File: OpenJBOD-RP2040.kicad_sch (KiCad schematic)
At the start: 55 parts, among them J1 ATX-24, J2 Bus_PCI_Express_x1, J3 Conn_02x02_Counter_Clockwise, J8 USB_B_Micro, J9 TEMP1, Q1 MMBT3904, Q2 MMBT3904, SW1 SW_Push, SW2 SW_Push, U1 RP2040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

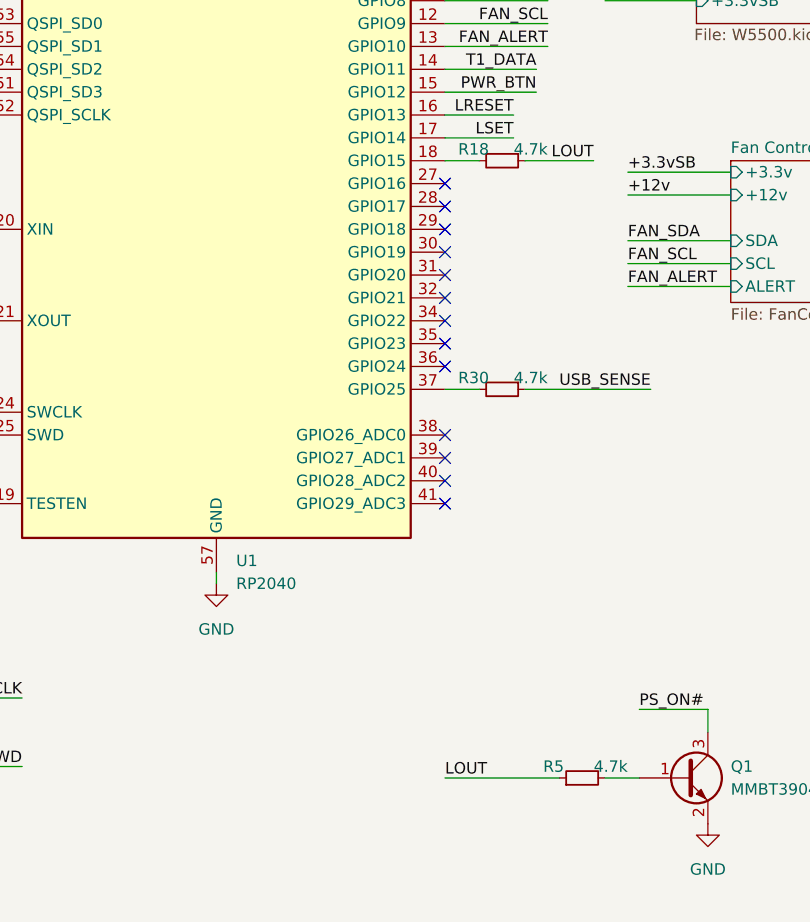
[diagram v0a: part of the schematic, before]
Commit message: added uart header
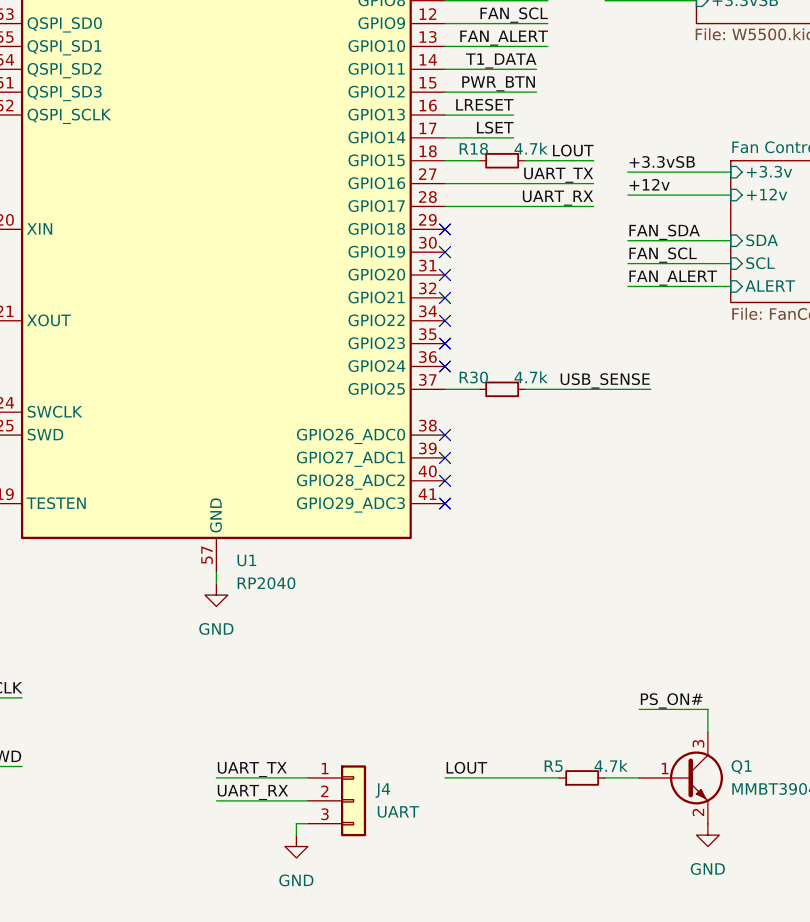
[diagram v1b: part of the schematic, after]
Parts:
- added J4: UART, Connector_PinHeader_2.54mm:PinHeader_1x03_P2.54mm_Vertical, symbol Connector_Generic:Conn_01x03
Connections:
- net GND: now also J4.3 (Pin_3)
- net UART_TX: now reaches U1.27 (GPIO16)
- net UART_TX: now also J4.1 (Pin_1)
- net UART_RX: now reaches U1.28 (GPIO17)
- net UART_RX: now also J4.2 (Pin_2)
- no-connect marks 34 -> 32
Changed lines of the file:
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@@
 	)
 	(no_connect
-		(at 96.52 116.84)
-	)
-	(no_connect
 		(at 247.65 35.56)
 	)
@@
 	)
 	(no_connect
-		(at 96.52 119.38)
-	)
-	(no_connect
 		(at 96.52 124.46)
 	)
@@
 	(wire
 		(pts
+			(xy 96.52 119.38) (xy 113.03 119.38)
+		)
+		(stroke
+			(width 0)
+			(type default)
+		)
+	)
+	(wire
+		(pts
 			(xy 242.57 17.78) (xy 260.35 17.78)
 		)
@@
 	(wire
 		(pts
+			(xy 96.52 116.84) (xy 113.03 116.84)
+		)
+		(stroke
+			(width 0)
+			(type default)
+		)
+	)
+	(wire
+		(pts
+			(xy 71.12 182.88) (xy 81.28 182.88)
+		)
+		(stroke
+			(width 0)
+			(type default)
+		)
+	)
+	(wire
+		(pts
 			(xy 105.41 114.3) (xy 113.03 114.3)
 		)
@@
 	(wire
 		(pts
+			(xy 80.01 189.23) (xy 80.01 187.96)
+		)
+		(stroke
+			(width 0)
+			(type default)
+		)
+	)
+	(wire
+		(pts
 			(xy 231.14 135.89) (xy 243.84 135.89)
 		)
@@
 	(wire
 		(pts
+			(xy 71.12 185.42) (xy 81.28 185.42)
+		)
+		(stroke
+			(width 0)
+			(type default)
+		)
+	)
+	(wire
+		(pts
 			(xy 96.52 81.28) (xy 124.46 81.28)
 		)
@@
 	(wire
 		(pts
+			(xy 80.01 187.96) (xy 81.28 187.96)
+		)
+		(stroke
+			(width 0)
+			(type default)
+		)
+	)
+	(wire
+		(pts
 			(xy 245.11 40.64) (xy 245.11 41.91)
 		)
@@
 		)
 	)
+	(label "UART_RX"
+		(at 113.03 119.38 180)
+		(fields_autoplaced yes)
+		(effects
+			(font
+				(size 1.27 1.27)
+			)
+			(justify right bottom)
+		)
+	)
 	(label "QSPI_SD2"
 		(at 210.82 82.55 0)
@@
 		)
 	)
+	(label "UART_TX"
+		(at 113.03 116.84 180)
+		(fields_autoplaced yes)
+		(effects
+			(font
+				(size 1.27 1.27)
+			)
+			(justify right bottom)
+		)
+	)
 	(label "PS_ON#"
 		(at 185.42 25.4 0)
@@
 		)
 	)
+	(label "UART_TX"
+		(at 71.12 182.88 0)
+		(fields_autoplaced yes)
+		(effects
+			(font
+				(size 1.27 1.27)
+			)
+			(justify left bottom)
+		)
+	)
 	(label "PWR_BTN"
 		(at 146.05 185.42 0)
@@
 		)
 	)
+	(label "UART_RX"
+		(at 71.12 185.42 0)
+		(fields_autoplaced yes)
+		(effects
+			(font
+				(size 1.27 1.27)
+			)
+			(justify left bottom)
+		)
+	)
 	(label "+12v"
 		(at 116.84 118.11 0)
@@
 	(symbol
 		(lib_id "power:GND")
+		(at 80.01 189.23 0)
+		(unit 1)
+		(exclude_from_sim no)
+		(in_bom yes)
+		(on_board yes)
+		(dnp no)
+		(property "Reference" "#PWR062"
+			(at 80.01 195.58 0)
+			(effects
+				(font
+					(size 1.27 1.27)
+				)
+				(hide yes)
+			)
+		)
+		(property "Value" "GND"
+			(at 80.01 194.31 0)
+			(effects
+				(font
+					(size 1.27 1.27)
+				)
+			)
+		)
+		(property "Footprint" ""
+			(at 80.01 189.23 0)
+			(effects
+				(font
+					(size 1.27 1.27)
+				)
+				(hide yes)
+			)
+		)
+		(property "Datasheet" ""
+			(at 80.01 189.23 0)
+			(effects
+				(font
+					(size 1.27 1.27)
+				)
+				(hide yes)
+			)
+		)
+		(property "Description" ""
+			(at 80.01 189.23 0)
+			(effects
+				(font
+					(size 1.27 1.27)
+				)
+				(hide yes)
+			)
+		)
+		(pin "1"
+		)
+		(instances
+			(project "OpenJBOD-RP2040"
+				(path "/341cb12b-c598-4bc6-a9bc-01f338de5a85"
+					(reference "#PWR062")
+					(unit 1)
+				)
+			)
+		)
+	)
+	(symbol
+		(lib_id "power:GND")
 		(at 189.23 73.66 0)
 		(unit 1)
@@
 					(unit 1)
 				)
+			)
+		)
+	)
+	(symbol
+		(lib_id "Connector_Generic:Conn_01x03")
+		(at 86.36 185.42 0)
+		(unit 1)
+		(exclude_from_sim no)
+		(in_bom yes)
+		(on_board yes)
+		(dnp no)
+		(fields_autoplaced yes)
+		(property "Reference" "J4"
+			(at 88.9 184.1499 0)
+			(effects
+				(font
+					(size 1.27 1.27)
+				)
+				(justify left)
+			)
+		)
+		(property "Value" "UART"
+			(at 88.9 186.6899 0)
+			(effects
+				(font
+					(size 1.27 1.27)
+				)
+				(justify left)
+			)
+		)
+		(property "Footprint" "Connector_PinHeader_2.54mm:PinHeader_1x03_P2.54mm_Vertical"
+			(at 86.36 185.42 0)
+			(effects
+				(font
+					(size 1.27 1.27)
+				)
+				(hide yes)
+			)
+		)
+		(property "Datasheet" "~"
+			(at 86.36 185.42 0)
+			(effects
+				(font
+					(size 1.27 1.27)
+				)
+				(hide yes)
+			)
+		)
+		(property "Description" "Generic connector, single row, 01x03, script generated (kicad-library-utils/schlib/autogen/connector/)"
+			(at 86.36 185.42 0)
+			(effects
+				(font
+					(size 1.27 1.27)
+				)
+				(hide yes)
+			)
+		)
+		(property "JLCPCB_PN" "C49257"
+			(at 86.36 185.42 0)
+			(effects
+				(font
+					(size 1.27 1.27)
+				)
+				(hide yes)
+			)
+		)
+		(pin "3"
+		)
+		(pin "1"
+		)
+		(pin "2"
+		)
+		(instances
+			(project "OpenJBOD-RP2040"
+				(path "/341cb12b-c598-4bc6-a9bc-01f338de5a85"
+					(reference "J4")
+					(unit 1)
+				)

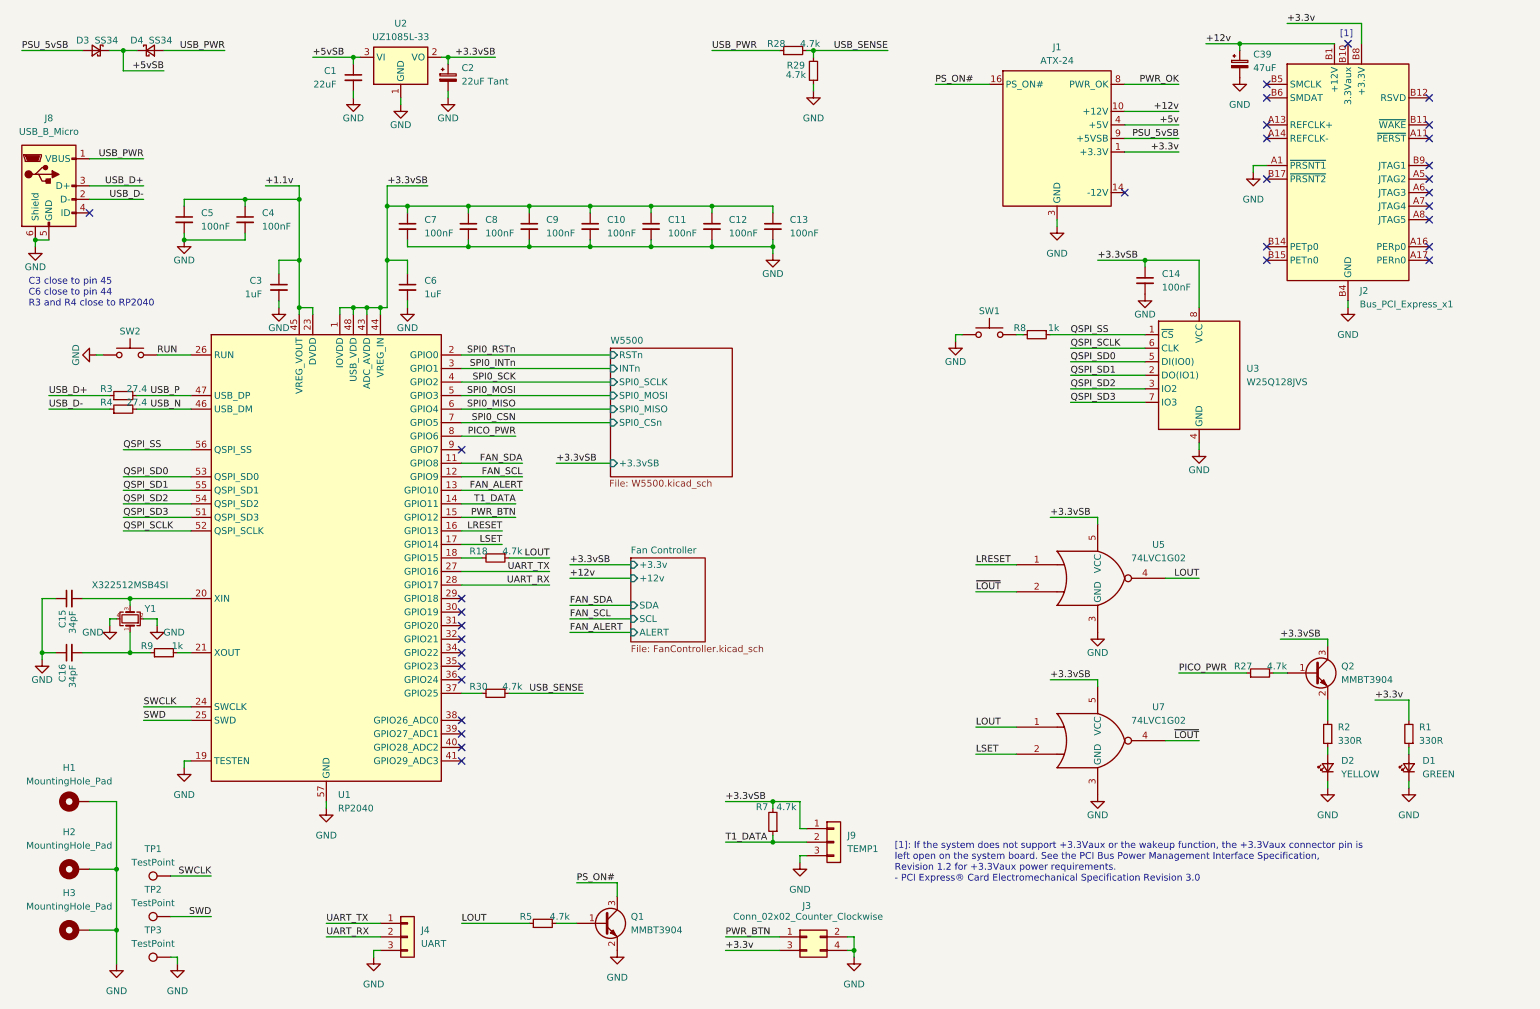
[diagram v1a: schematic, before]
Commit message: Rev4
Bunch of small changes, namely:
Add onboard DS18B20 probe for more accurate temp readings without external hardware.
Rename T1DATA to T2DATA to still allow external probes.
Add USB power sensing circuit.
Add SR latch for PS_ON# handling
Add J4 UART header.
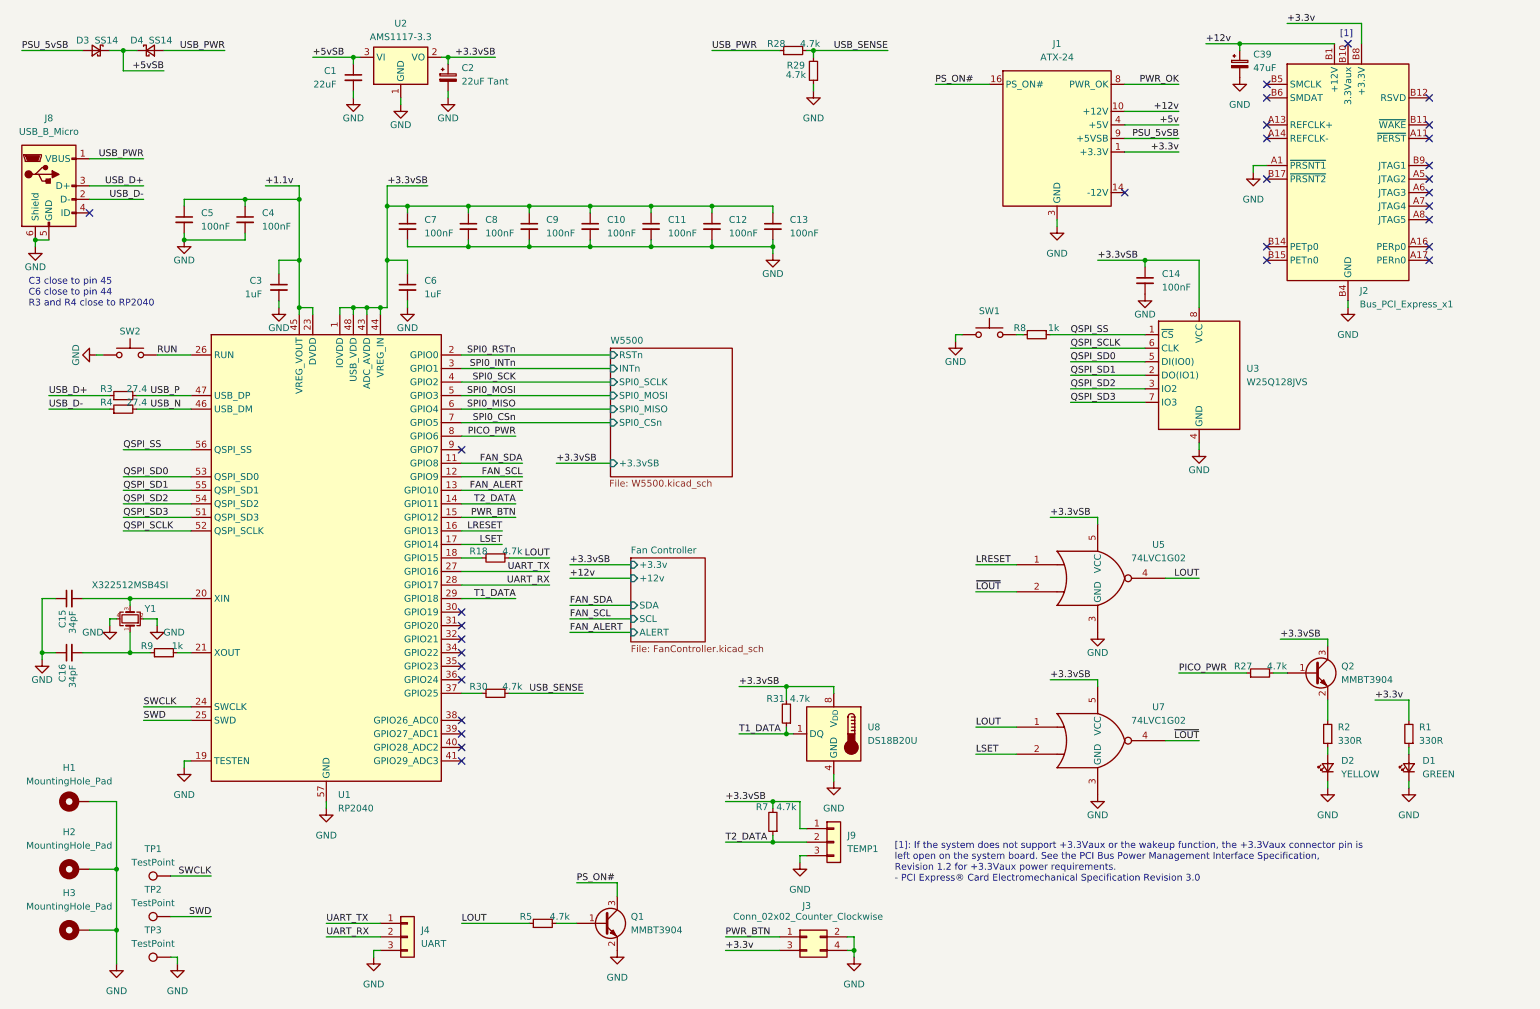
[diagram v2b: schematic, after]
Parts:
- added R31: 4.7k, Resistor_SMD:R_0402_1005Metric, symbol Device:R_Small
- added U8: DS18B20U, Package_SO:MSOP-8_3x3mm_P0.65mm, symbol Sensor_Temperature:DS18B20U
- D3, D4: value SS34 -> SS14
- J1: footprint Connector_Molex:Molex_Mini-Fit_Jr_5566-24A_2x12_P4.20mm_Vertical -> OpenJBOD_Library:CONN-TH_M4202V-2X12P
- U2: value UZ1085L-33 -> AMS1117-3.3; footprint Package_TO_SOT_SMD:TO-252-2 -> Package_TO_SOT_SMD:SOT-223-3_TabPin2; JLCPCB_PN C125622 -> (none)
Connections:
- net +3.3vSB: now also R31.2, U8.8 (V_{DD})
- net GND: now also U8.4 (GND)
- net T1_DATA: now also U1.29 (GPIO18), R31.1, U8.1 (DQ); no longer J9.2 (Pin_2), R7.1, U1.14 (GPIO11)
- net SPI0_CSN renamed SPI0_CSn
- new net T2_DATA: J9.2 (Pin_2), R7.1, U1.14 (GPIO11)
- no-connect marks 32 -> 31

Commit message: rev4 order version added side-mounted IO to the panel so an IO shield could theoretically be made added step models cleaned up footprints
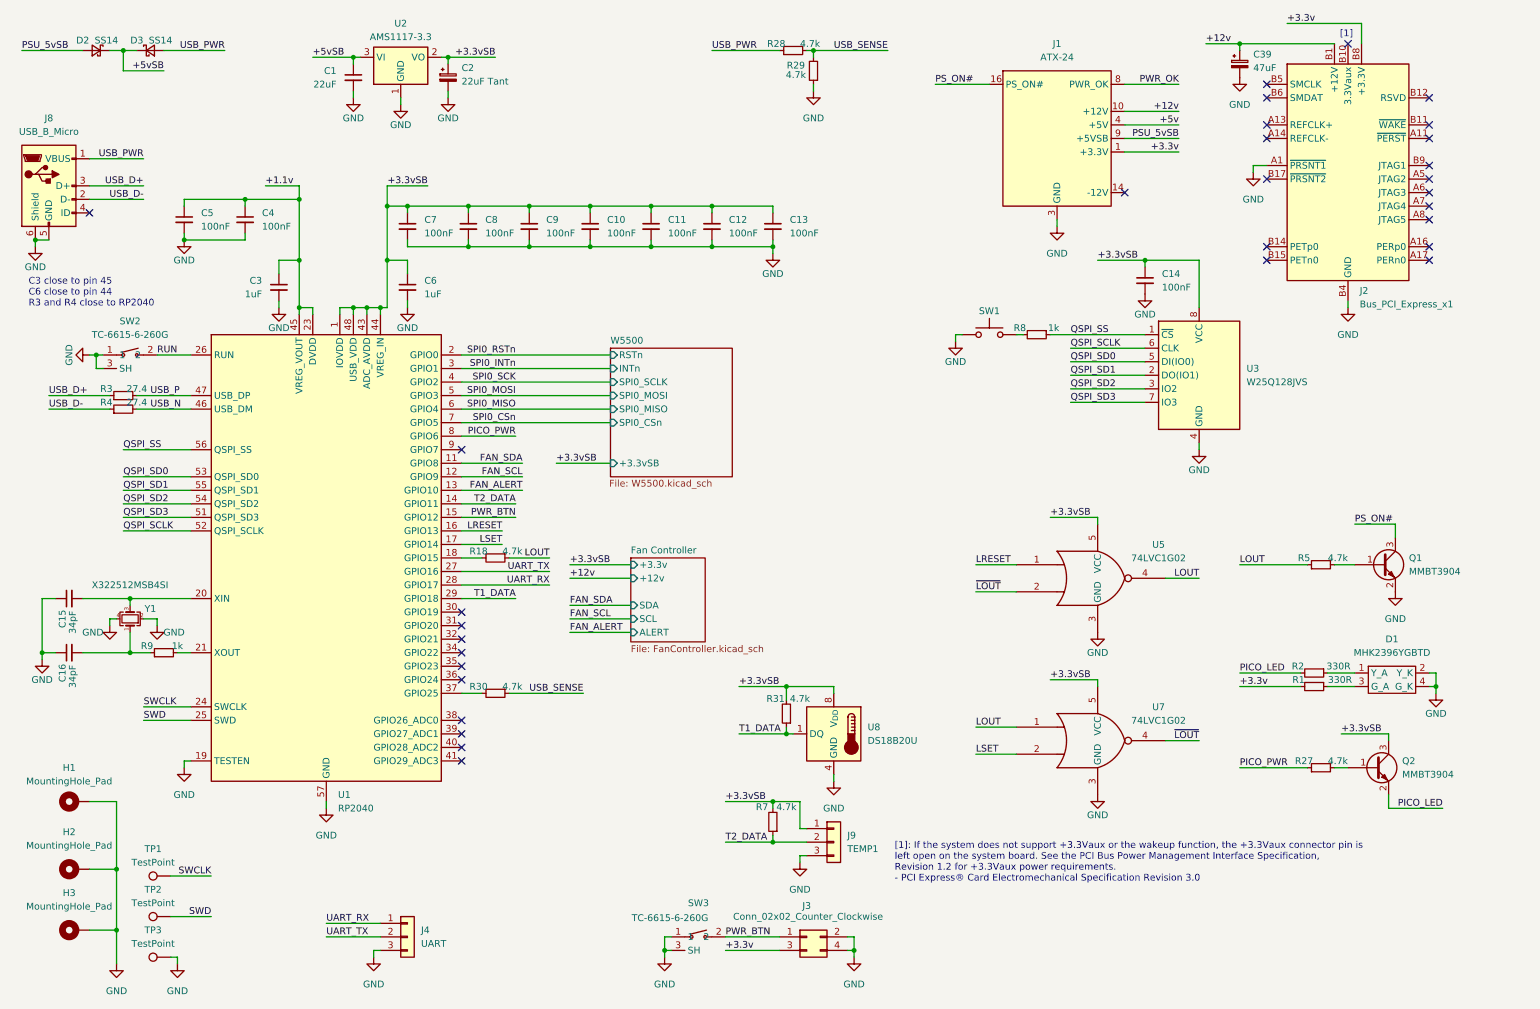
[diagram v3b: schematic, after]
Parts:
- removed D1: GREEN, LED_SMD:LED_0805_2012Metric, symbol Device:LED_Small
- removed D2: YELLOW, LED_SMD:LED_0805_2012Metric, symbol Device:LED_Small
- removed SW2: SW_Push, Button_Switch_SMD:SW_Push_1P1T_XKB_TS-1187A, symbol Switch:SW_Push
- added D1: MHK2396YGBTD, OpenJBOD_Library:LED-TH_MHK2396YGBTD, symbol OpenJBOD:MHK2396YGBTD
- added SW2, SW3: TC-6615-6-260G, OpenJBOD_Library:KEY-TH_TC-6615-6-160G, symbol OpenJBOD:TC-6615-6-260G
- J4: footprint Connector_PinHeader_2.54mm:PinHeader_1x03_P2.54mm_Vertical -> Connector_PinHeader_2.54mm:PinHeader_1x03_P2.54mm_Horizontal; JLCPCB_PN C49257 -> C92159
- renumbered D3 to D2, D4 to D3
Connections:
- net GND: now also D1.2 (Y_K), D1.4 (G_K), SW2.1, SW2.3 (SH), SW2.4 (SH), SW3.1, SW3.3 (SH), SW3.4 (SH)
- net PWR_BTN: now also SW3.2
- net RUN: now also SW2.2
- net UART_RX: now also J4.1 (Pin_1); no longer J4.2 (Pin_2)
- net UART_TX: now also J4.2 (Pin_2); no longer J4.1 (Pin_1)
- net at R1.1: now also D1.3 (G_A)
- net at R2.1: now also D1.1 (Y_A)
- net PICO_LED: now reaches Q2.2 (E), R2.2
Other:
- moved on the sheet: Q1, Q2, R1, R2, R27, R5
